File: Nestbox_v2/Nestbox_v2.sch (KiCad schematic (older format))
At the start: 0 parts

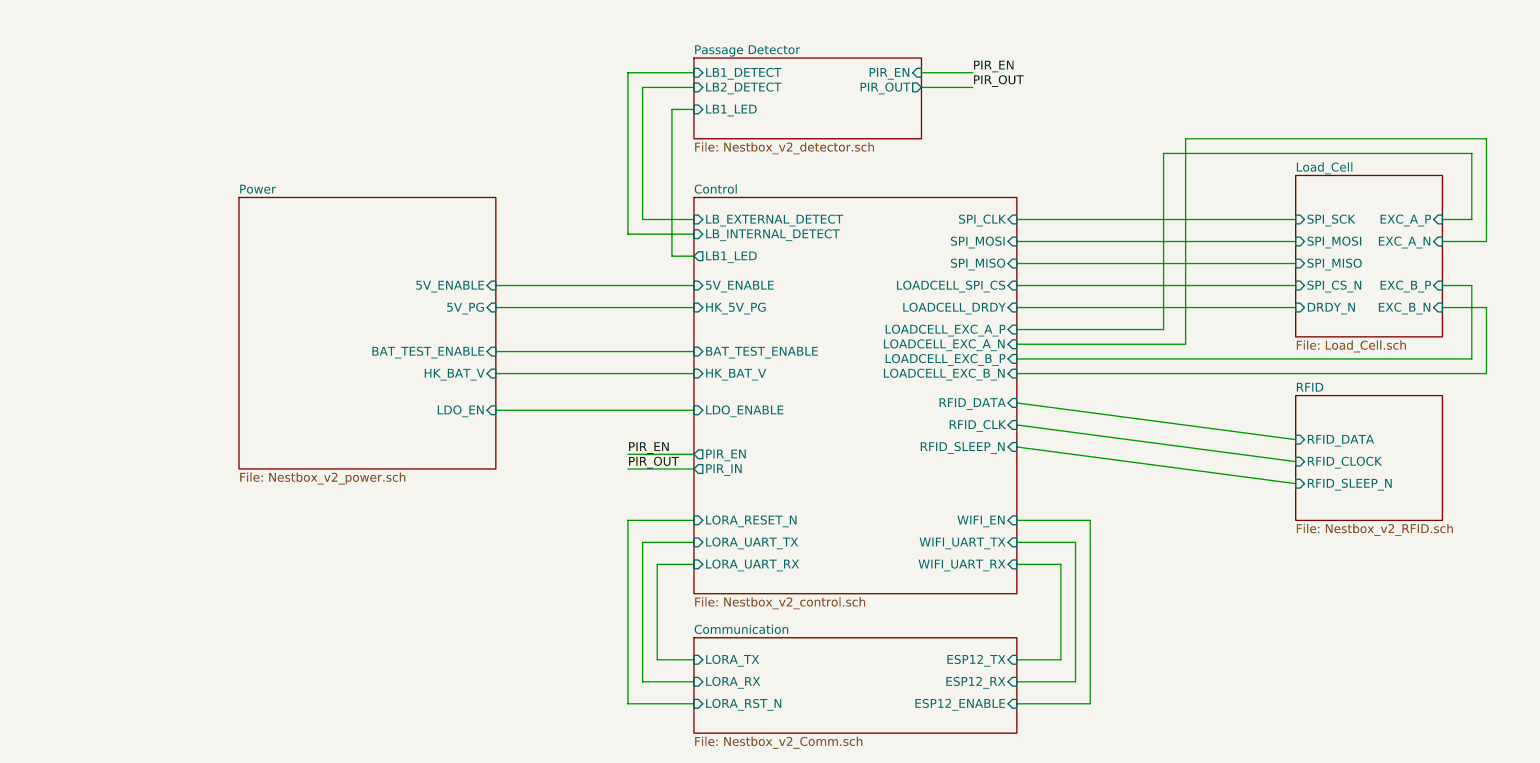
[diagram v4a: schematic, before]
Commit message: all footprints assigned except mosfets; final connectors and their locatino, started component placement
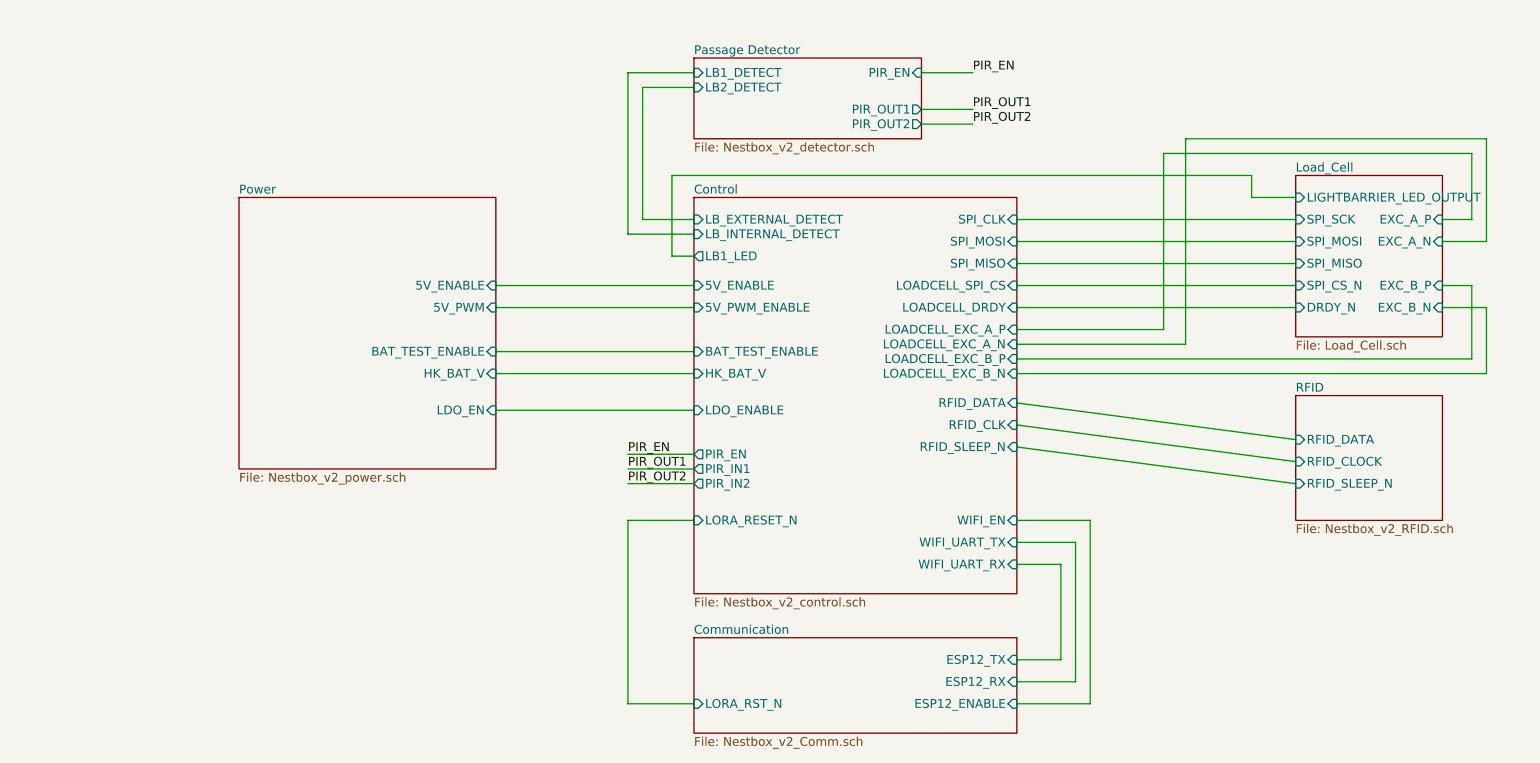
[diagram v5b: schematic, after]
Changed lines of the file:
@@
 EESchema Schematic File Version 2
-LIBS:Nestbox_v2-rescue
-LIBS:Octanis3
 LIBS:power
 LIBS:device
-LIBS:switches
-LIBS:relays
-LIBS:motors
 LIBS:transistors
 LIBS:conn
@@
 LIBS:contrib
 LIBS:valves
-LIBS:SeeedOPL-Capacitor-2016
-LIBS:SeeedOPL-Connector-2016
-LIBS:SeeedOPL-Crystal Oscillator-2016
-LIBS:SeeedOPL-Diode-2016
-LIBS:SeeedOPL-Display-2016
-LIBS:SeeedOPL-Fuse-2016
-LIBS:SeeedOPL-IC-2016
-LIBS:SeeedOPL-Inductor-2016
-LIBS:SeeedOPL-LED-2016
-LIBS:SeeedOPL-Relay-2016
-LIBS:SeeedOPL-Resistor-2016
-LIBS:SeeedOPL-Sensor-2016
-LIBS:SeeedOPL-Switch-2016
-LIBS:SeeedOPL-Transistor-2016
+LIBS:Octanis3
 LIBS:Nestbox_v2-cache
 EELAYER 25 0
@@
 F4 "LDO_EN" I R 4100 3750 60
 F5 "BAT_TEST_ENABLE" I R 4100 3350 60
-F6 "5V_PG" I R 4100 3050 60
+F6 "5V_PWM" I R 4100 3050 60
 $EndSheet
 $Sheet
@@
 F14 "LORA_RESET_N" I L 5450 4500 60
 F15 "WIFI_EN" I R 7650 4500 60
-F16 "LORA_UART_TX" I L 5450 4650 60
-F17 "LORA_UART_RX" I L 5450 4800 60
-F18 "LOADCELL_EXC_A_P" I R 7650 3200 60
-F19 "LOADCELL_EXC_A_N" I R 7650 3300 60
-F20 "LOADCELL_EXC_B_P" I R 7650 3400 60
-F21 "LOADCELL_EXC_B_N" I R 7650 3500 60
-F22 "RFID_SLEEP_N" I R 7650 4000 60
-F23 "BAT_TEST_ENABLE" I L 5450 3350 60
-F24 "HK_5V_PG" I L 5450 3050 60
-F25 "LB_INTERNAL_DETECT" I L 5450 2550 60
-F26 "LB_EXTERNAL_DETECT" I L 5450 2450 60
-F27 "LB1_LED" O L 5450 2700 60
-F28 "PIR_EN" O L 5450 4050 60
-F29 "PIR_IN" O L 5450 4150 60
+F16 "LOADCELL_EXC_A_P" I R 7650 3200 60
+F17 "LOADCELL_EXC_A_N" I R 7650 3300 60
+F18 "LOADCELL_EXC_B_P" I R 7650 3400 60
+F19 "LOADCELL_EXC_B_N" I R 7650 3500 60
+F20 "RFID_SLEEP_N" I R 7650 4000 60
+F21 "BAT_TEST_ENABLE" I L 5450 3350 60
+F22 "LB_INTERNAL_DETECT" I L 5450 2550 60
+F23 "LB_EXTERNAL_DETECT" I L 5450 2450 60
+F24 "LB1_LED" O L 5450 2700 60
+F25 "PIR_EN" O L 5450 4050 60
+F26 "5V_PWM_ENABLE" I L 5450 3050 60
+F27 "PIR_IN1" O L 5450 4150 60
+F28 "PIR_IN2" O L 5450 4250 60
 $EndSheet
 $Sheet
@@
 F1 "Nestbox_v2_detector.sch" 60
 F2 "LB1_DETECT" I L 5450 1450 60
-F3 "LB1_LED" I L 5450 1700 60
-F4 "LB2_DETECT" I L 5450 1550 60
-F5 "PIR_EN" I R 7000 1450 60
-F6 "PIR_OUT" O R 7000 1550 60
+F3 "LB2_DETECT" I L 5450 1550 60
+F4 "PIR_EN" I R 7000 1450 60
+F6 "PIR_OUT1" O R 7000 1700 60
+F7 "PIR_OUT2" O R 7000 1800 60
 $EndSheet
 $Sheet
@@
 F3 "ESP12_RX" I R 7650 5600 60
 F4 "ESP12_ENABLE" I R 7650 5750 60
-F5 "LORA_RX" I L 5450 5600 60
-F6 "LORA_TX" I L 5450 5450 60
-F7 "LORA_RST_N" I L 5450 5750 60
+F5 "LORA_RST_N" I L 5450 5750 60
 $EndSheet
 $Sheet
@@
 F9 "EXC_B_N" I R 10550 3050 60
 F10 "EXC_B_P" I R 10550 2900 60
+F11 "LIGHTBARRIER_LED_OUTPUT" I L 9550 2300 60
 $EndSheet
 Wire Wire Line
@@
 Wire Wire Line
 	7950 5450 7650 5450
-Wire Wire Line
-	5450 4800 5200 4800
-Wire Wire Line
-	5200 4800 5200 5450
-Wire Wire Line
-	5200 5450 5450 5450
-Wire Wire Line
-	5450 4650 5100 4650
-Wire Wire Line
-	5100 4650 5100 5600
-Wire Wire Line
-	5100 5600 5450 5600
 Wire Wire Line
 	5450 4500 5000 4500
@@
 	5100 1550 5450 1550
 Wire Wire Line
-	5450 1700 5300 1700
-Wire Wire Line
-	5300 1700 5300 2700
-Wire Wire Line
 	5300 2700 5450 2700
 Wire Wire Line
@@
 Wire Wire Line
 	7000 1450 7350 1450
-Wire Wire Line
-	7000 1550 7350 1550
 Text Label 7350 1450 0    60   ~ 0
 PIR_EN
-Text Label 7350 1550 0    60   ~ 0
-PIR_OUT
+Text Label 7350 1700 0    60   ~ 0
+PIR_OUT1
 Text Label 5000 4050 0    60   ~ 0
 PIR_EN
 Text Label 5000 4150 0    60   ~ 0
-PIR_OUT
+PIR_OUT1
+Wire Wire Line
+	5300 2700 5300 2150
+Wire Wire Line
+	5300 2150 9250 2150
+Wire Wire Line
+	9250 2150 9250 2300
+Wire Wire Line
+	9250 2300 9550 2300
+Text Label 5000 4250 0    60   ~ 0
+PIR_OUT2
+Wire Wire Line
+	5450 4250 5000 4250
+Wire Wire Line
+	7000 1700 7350 1700
+Wire Wire Line
+	7000 1800 7350 1800
+Text Label 7350 1800 0    60   ~ 0
+PIR_OUT2
 $EndSCHEMATC
